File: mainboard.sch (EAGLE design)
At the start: 69 parts, among them J1 POWER_JACKPTH_LOCK, T1 SINGLE_NCHAN_FET, T2 MOSFET_PCHAN_20A, T3 SINGLE_NCHAN_FET, T4 MOSFET_PCHAN_20A, T5 SINGLE_NCHAN_FET, T6 MOSFET_PCHAN_20A, T7 MOSFET_PCHAN_20A, T8 SINGLE_NCHAN_FET, U1 MURATA_REG_OKL-T3-W12, U2 TEENSY_3.0+4, U3 RFM23BP, U4 HMC5883LSMD, U5 ITG-3200, U7 CURRENT_MAX4372, U8 CURRENT_MAX4372

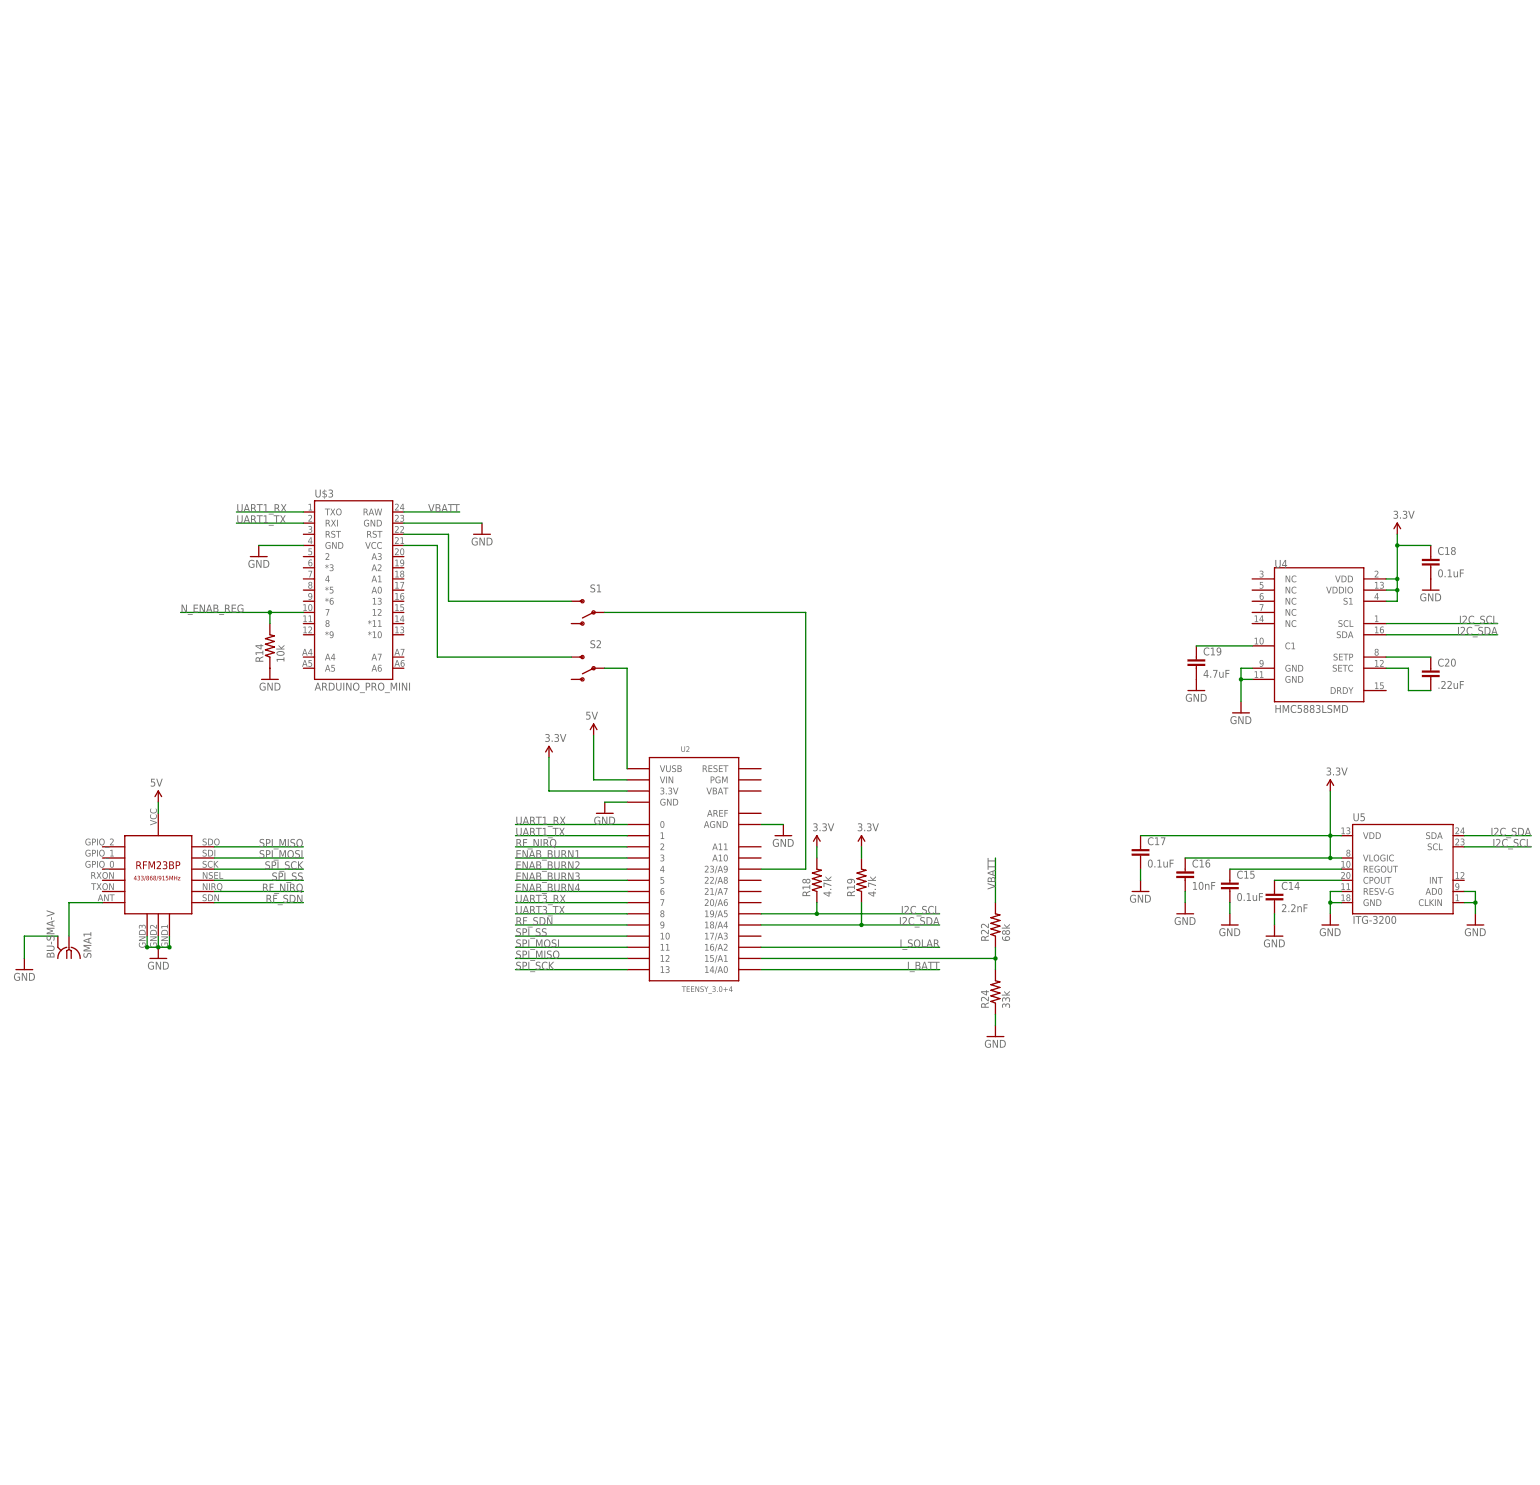
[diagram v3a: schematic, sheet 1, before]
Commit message: Fixed charging jack on schematic
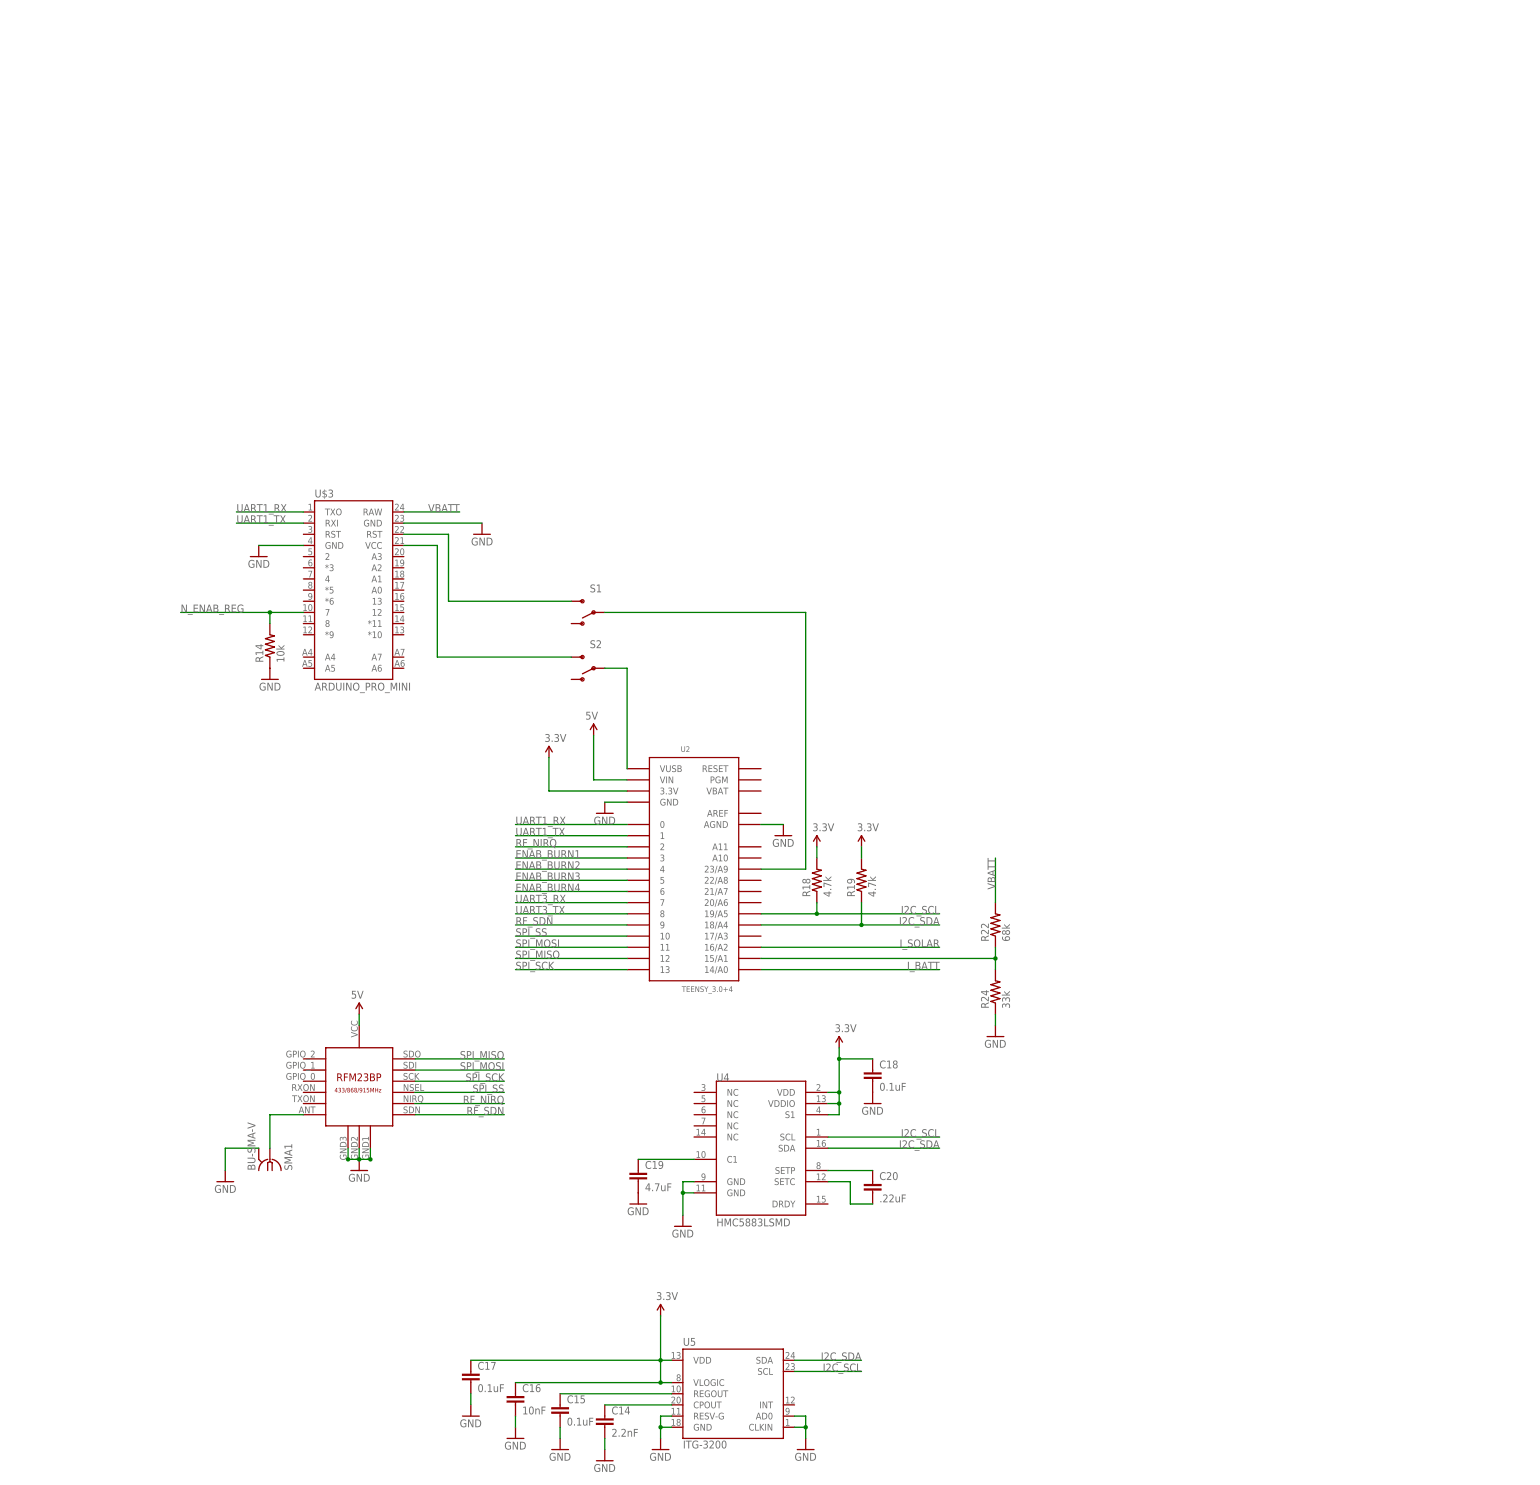
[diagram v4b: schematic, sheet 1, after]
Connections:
- net GND: no longer J1.GND, J1.GNDBREAK
- net N$1: now also J1.GND, J1.GNDBREAK
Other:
- moved on the sheet: C1, C13, C14, C15, C16, C17, C18, C19, C2, C20, C3, R20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

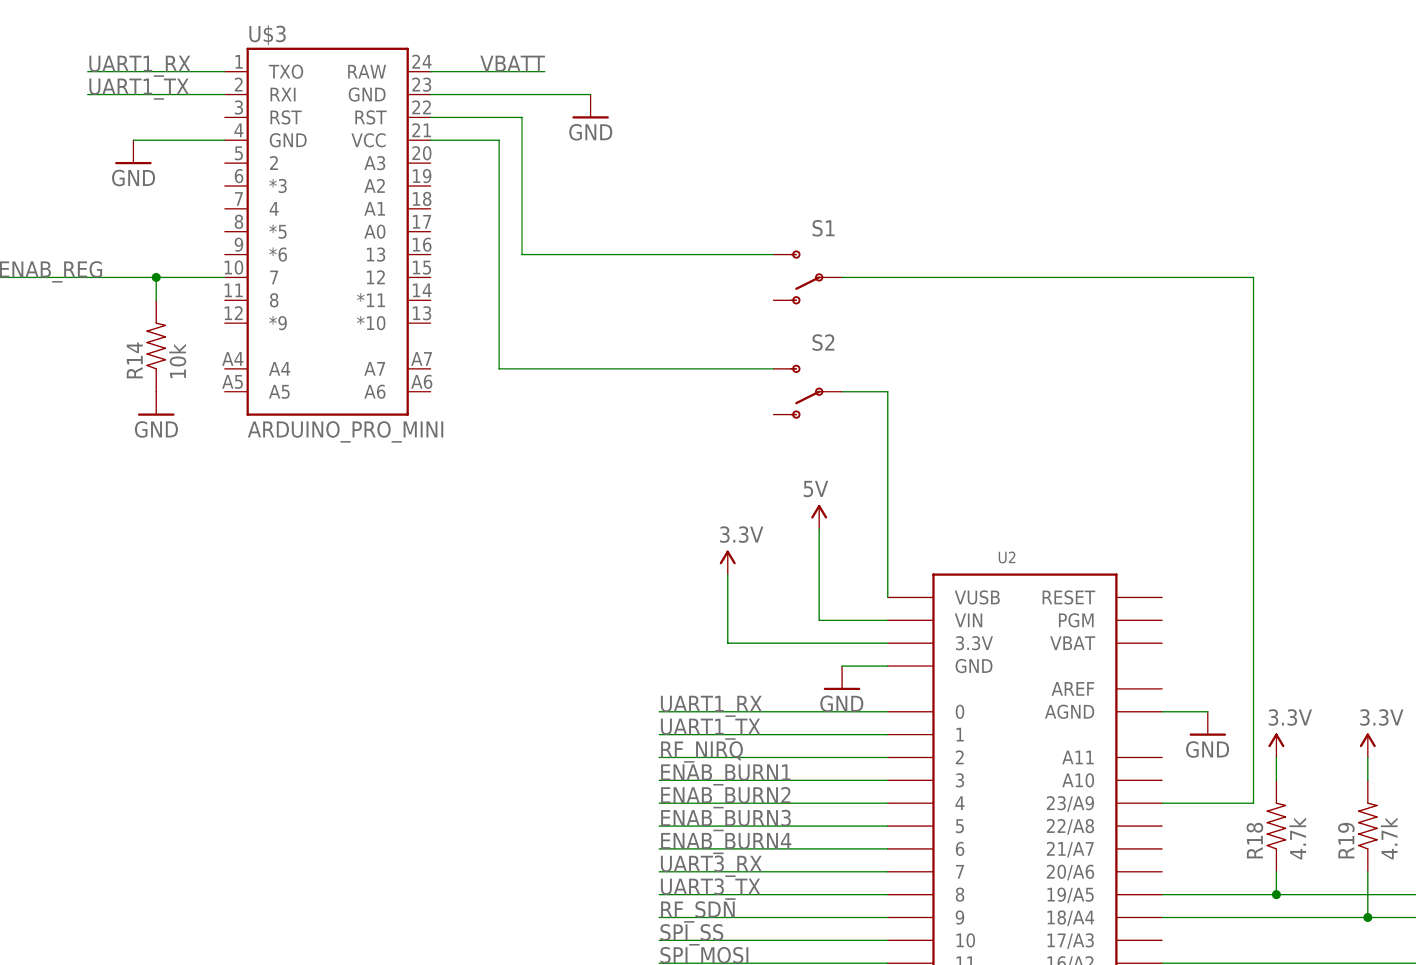
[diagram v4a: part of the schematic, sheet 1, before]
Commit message: DPDT Switch for programming mode
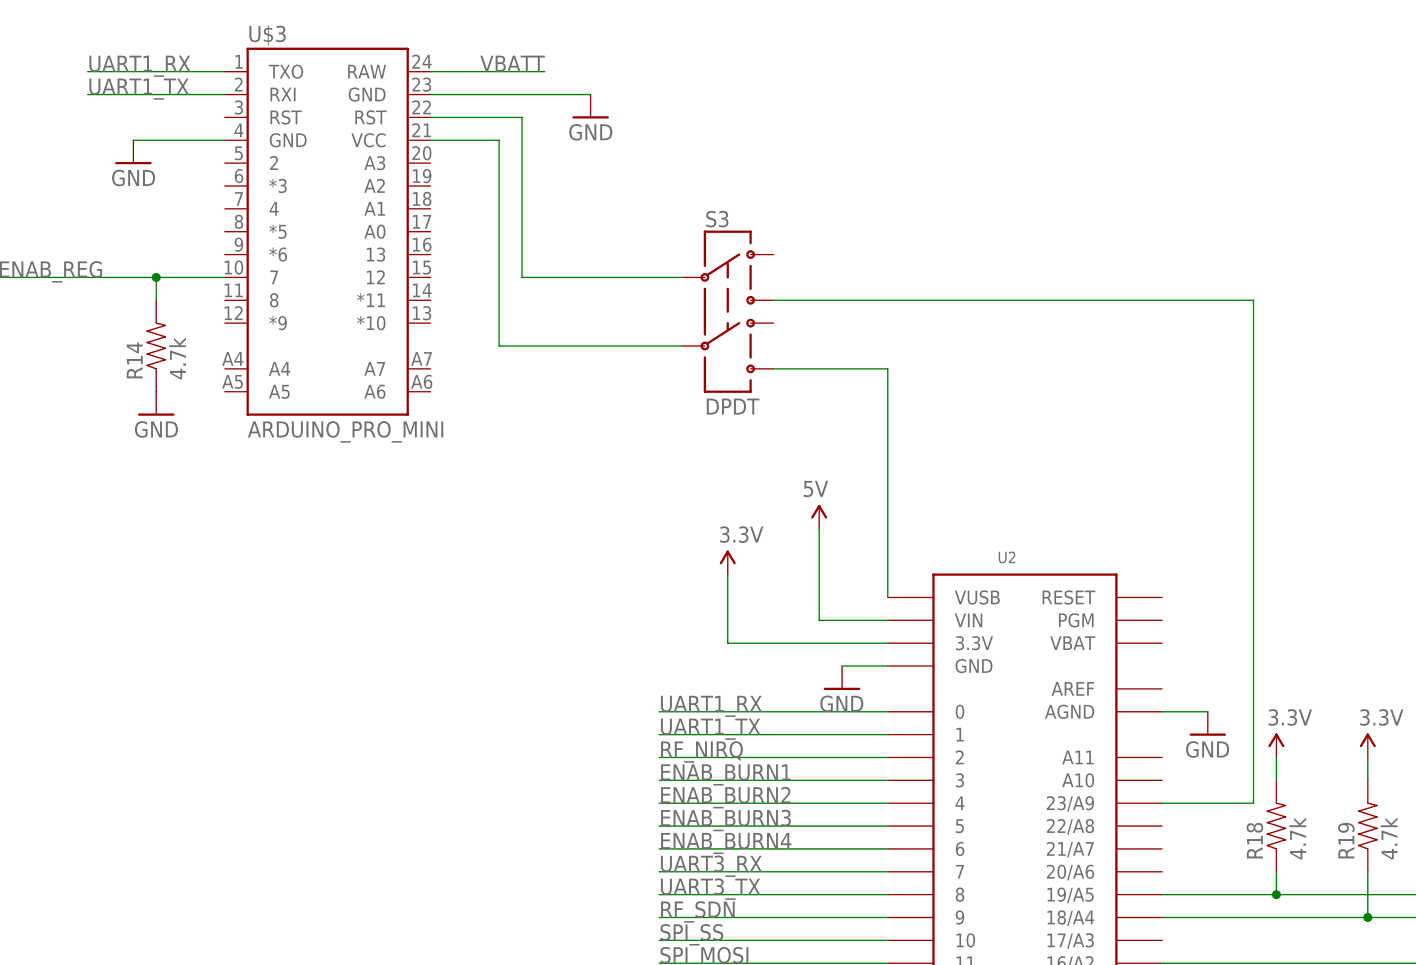
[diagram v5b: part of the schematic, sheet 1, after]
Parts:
- removed S1, S2: (no value), SparkFun-Electromechanical:SWITCH-SPDTPTH
- added S3: DPDT, SparkFun-Electromechanical:SWITCH-DPDTAYZ0202
- R14: value 10k -> 4.7k
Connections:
- net N$11: now also S3.3; no longer S1.P
- net N$13: now also S3.6; no longer S2.P
- net PGM_RST: now also S3.2; no longer S1.S
- net PGM_VCC: now also S3.5; no longer S2.S
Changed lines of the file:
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@@
 <part name="GND18" library="SparkFun" deviceset="GND" device=""/>
 <part name="U$3" library="SparkFun-Boards" deviceset="ARDUINO_PRO_MINI" device=""/>
-<part name="R14" library="SparkFun-Resistors" deviceset="RESISTOR" device="0805-RES" value="10k"/>
+<part name="R14" library="SparkFun-Resistors" deviceset="RESISTOR" device="0805-RES" value="4.7k"/>
 <part name="GND19" library="SparkFun" deviceset="GND" device=""/>
-<part name="S1" library="SparkFun-Electromechanical" deviceset="SWITCH-SPDT" device="PTH"/>
-<part name="S2" library="SparkFun-Electromechanical" deviceset="SWITCH-SPDT" device="PTH"/>
+<part name="S3" library="SparkFun-Electromechanical" deviceset="SWITCH-DPDT" device="AYZ0202" value="DPDT"/>
 </parts>
 <sheets>
@@
 <instance part="R14" gate="G$1" x="-30.48" y="40.64" rot="R90"/>
 <instance part="GND19" gate="1" x="-30.48" y="33.02" rot="MR0"/>
-<instance part="S1" gate="1" x="43.18" y="48.26" rot="R180"/>
-<instance part="S2" gate="1" x="43.18" y="35.56" rot="R180"/>
+<instance part="S3" gate="G$1" x="33.02" y="45.72"/>
 </instances>
 <busses>
@@
 <pinref part="U$3" gate="G$1" pin="VCC"/>
 <wire x1="0" y1="63.5" x2="7.62" y2="63.5" width="0.1524" layer="91"/>
-<wire x1="7.62" y1="63.5" x2="7.62" y2="38.1" width="0.1524" layer="91"/>
-<pinref part="S2" gate="1" pin="S"/>
-<wire x1="38.1" y1="38.1" x2="7.62" y2="38.1" width="0.1524" layer="91"/>
+<wire x1="7.62" y1="63.5" x2="7.62" y2="40.64" width="0.1524" layer="91"/>
+<wire x1="27.94" y1="40.64" x2="7.62" y2="40.64" width="0.1524" layer="91"/>
+<pinref part="S3" gate="G$1" pin="5"/>
 </segment>
 </net>
 <net name="N$11" class="0">
 <segment>
-<wire x1="91.44" y1="48.26" x2="91.44" y2="-10.16" width="0.1524" layer="91"/>
+<wire x1="91.44" y1="45.72" x2="91.44" y2="-10.16" width="0.1524" layer="91"/>
 <pinref part="U2" gate="G$1" pin="23/A9"/>
 <wire x1="91.44" y1="-10.16" x2="81.28" y2="-10.16" width="0.1524" layer="91"/>
-<pinref part="S1" gate="1" pin="P"/>
-<wire x1="45.72" y1="48.26" x2="91.44" y2="48.26" width="0.1524" layer="91"/>
+<wire x1="38.1" y1="45.72" x2="91.44" y2="45.72" width="0.1524" layer="91"/>
+<pinref part="S3" gate="G$1" pin="3"/>
 </segment>
 </net>
@@
 <pinref part="U$3" gate="G$1" pin="RST@2"/>
 <wire x1="0" y1="66.04" x2="10.16" y2="66.04" width="0.1524" layer="91"/>
-<wire x1="10.16" y1="66.04" x2="10.16" y2="50.8" width="0.1524" layer="91"/>
-<wire x1="10.16" y1="50.8" x2="38.1" y2="50.8" width="0.1524" layer="91"/>
-<pinref part="S1" gate="1" pin="S"/>
+<wire x1="10.16" y1="66.04" x2="10.16" y2="48.26" width="0.1524" layer="91"/>
+<wire x1="10.16" y1="48.26" x2="27.94" y2="48.26" width="0.1524" layer="91"/>
+<pinref part="S3" gate="G$1" pin="2"/>
 </segment>
 </net>
 <net name="N$13" class="0">
 <segment>
-<pinref part="S2" gate="1" pin="P"/>
 <pinref part="U2" gate="G$1" pin="VUSB"/>
-<wire x1="45.72" y1="35.56" x2="50.8" y2="35.56" width="0.1524" layer="91"/>
-<wire x1="50.8" y1="35.56" x2="50.8" y2="12.7" width="0.1524" layer="91"/>
-</segment>
-</net>
+<wire x1="50.8" y1="38.1" x2="50.8" y2="12.7" width="0.1524" layer="91"/>
+<pinref part="S3" gate="G$1" pin="6"/>
+<wire x1="50.8" y1="38.1" x2="38.1" y2="38.1" width="0.1524" layer="91"/>
+</segment>
+</net>
